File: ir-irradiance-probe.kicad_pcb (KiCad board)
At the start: 2 copper layers, 50 x 50 mm, 54 parts, among them J1 USB-C_UJC-HP-3-SMT-TR, J2 SM04B-SRSS-TB-LF-SN, J3 PinHeader_1x2_P2.54mm_Drill1.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, J4 Conn_BNC_031-70526-21, SW1 MSS3-V-T_R, U1 TLV70033_SC70, U2 AD8604ARUZ, U3 ADC101C027CIMK

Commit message: [#47284] Create local components library
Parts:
- C1, C10, C11, C2, C3, C4, C5, C7, C8, C9: footprint antmicro-footprints:C_0402_1005Metric -> ir-irradiance-probe-footprints:C_0402_1005Metric
- C6: footprint antmicro-footprints:C_0603_1608Metric -> ir-irradiance-probe-footprints:C_0603_1608Metric
- D1, D2, D3, D6: footprint antmicro-footprints:SOD-523 -> ir-irradiance-probe-footprints:SOD-523
- D4, D5: footprint antmicro-footprints:TPD2E009DRTR -> ir-irradiance-probe-footprints:TPD2E009DRTR
- D7: footprint antmicro-footprints:LED_0603_1608Metric_G -> ir-irradiance-probe-footprints:LED_0603_1608Metric_G
- D8, D9: footprint antmicro-footprints:Photodiode_SMD_4.2x5mm_TEMD -> ir-irradiance-probe-footprints:Photodiode_SMD_4.2x5mm_TEMD
- J1: footprint antmicro-footprints:USB-C_UJC-HP-3-SMT-TR -> ir-irradiance-probe-footprints:USB-C_UJC-HP-3-SMT-TR
- J2: footprint antmicro-footprints:SM04B-SRSS-TB-LF-SN -> ir-irradiance-probe-footprints:SM04B-SRSS-TB-LF-SN
- J3: footprint antmicro-footprints:PinHeader_1x2_P2.54_Drill0.9mm -> ir-irradiance-probe-footprints:PinHeader_1x2_P2.54_Drill0.9mm
- J4: footprint antmicro-footprints:Conn_BNC_031-70526-21 -> ir-irradiance-probe-footprints:Conn_BNC_031-70526-21
- L1: footprint antmicro-footprints:L_0603_1608Metric -> ir-irradiance-probe-footprints:L_0603_1608Metric
- MP1, MP2, MP3, MP4: footprint antmicro-footprints:mounting-hole-2.75mm-M2.5_D6.2mm_PTH -> ir-irradiance-probe-footprints:mounting-hole-2.75mm-M2.5_D6.2mm_PTH
- N1: footprint antmicro-footprints:antmicro-logo_scaled_20mm -> ir-irradiance-probe-footprints:antmicro-logo_scaled_20mm
- N2: footprint antmicro-footprints:oshw-logo -> ir-irradiance-probe-footprints:oshw-logo
- POT1: footprint antmicro-footprints:PTD902-1015K-B104 -> ir-irradiance-probe-footprints:PTD902-1015K-B104
- R1, R10, R11, R12, R13, R2, R3, R4, R5, R6, R7, R8, R9: footprint antmicro-footprints:R_0402_1005Metric -> ir-irradiance-probe-footprints:R_0402_1005Metric
- SW1: footprint antmicro-footprints:Switch_Slide_MSS3 -> ir-irradiance-probe-footprints:Switch_Slide_MSS3
- U1: footprint antmicro-footprints:SC-70-5 -> ir-irradiance-probe-footprints:SC-70-5
- U2: footprint antmicro-footprints:TSSOP-14_4.4x5mm_P0.65mm -> ir-irradiance-probe-footprints:TSSOP-14_4.4x5mm_P0.65mm
- U3: footprint antmicro-footprints:SOT-23-6 -> ir-irradiance-probe-footprints:SOT-23-6

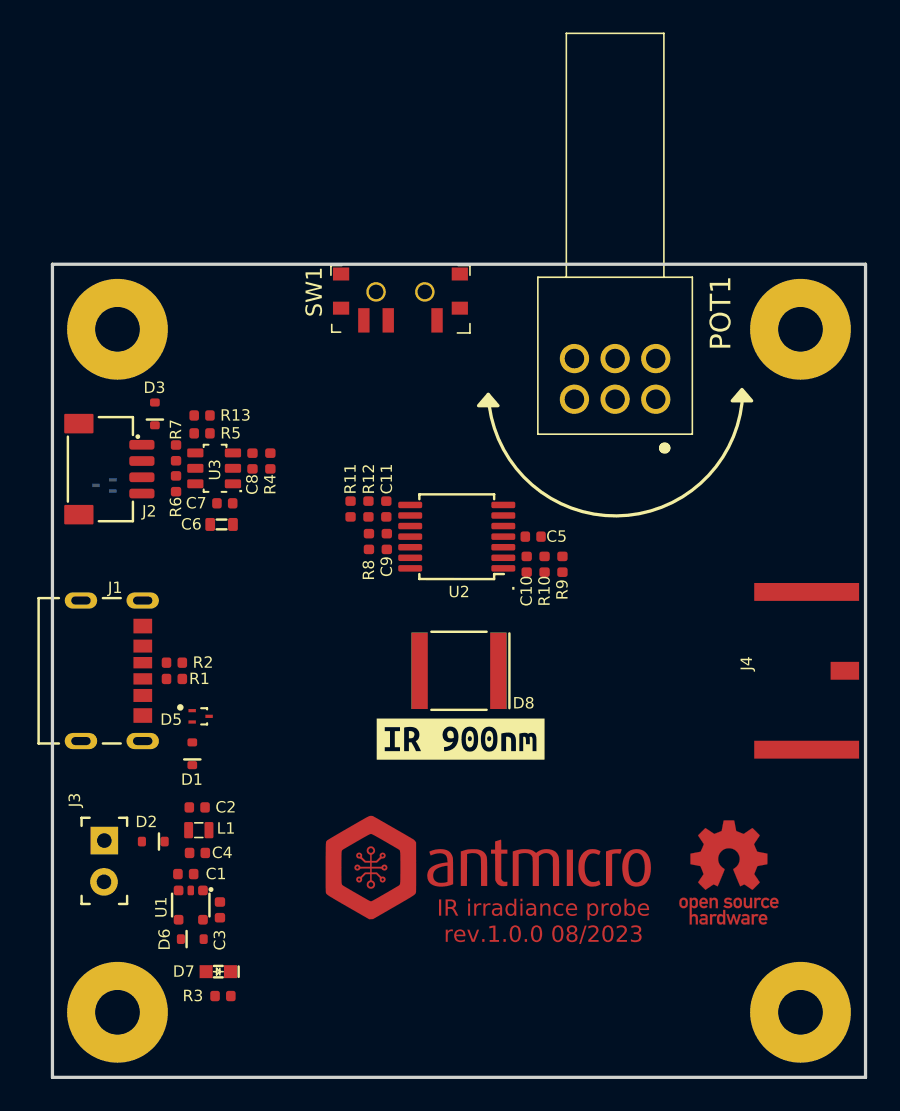
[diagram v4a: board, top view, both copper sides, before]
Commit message: [#47284] Rework PCB layout to fit 4x4cm board
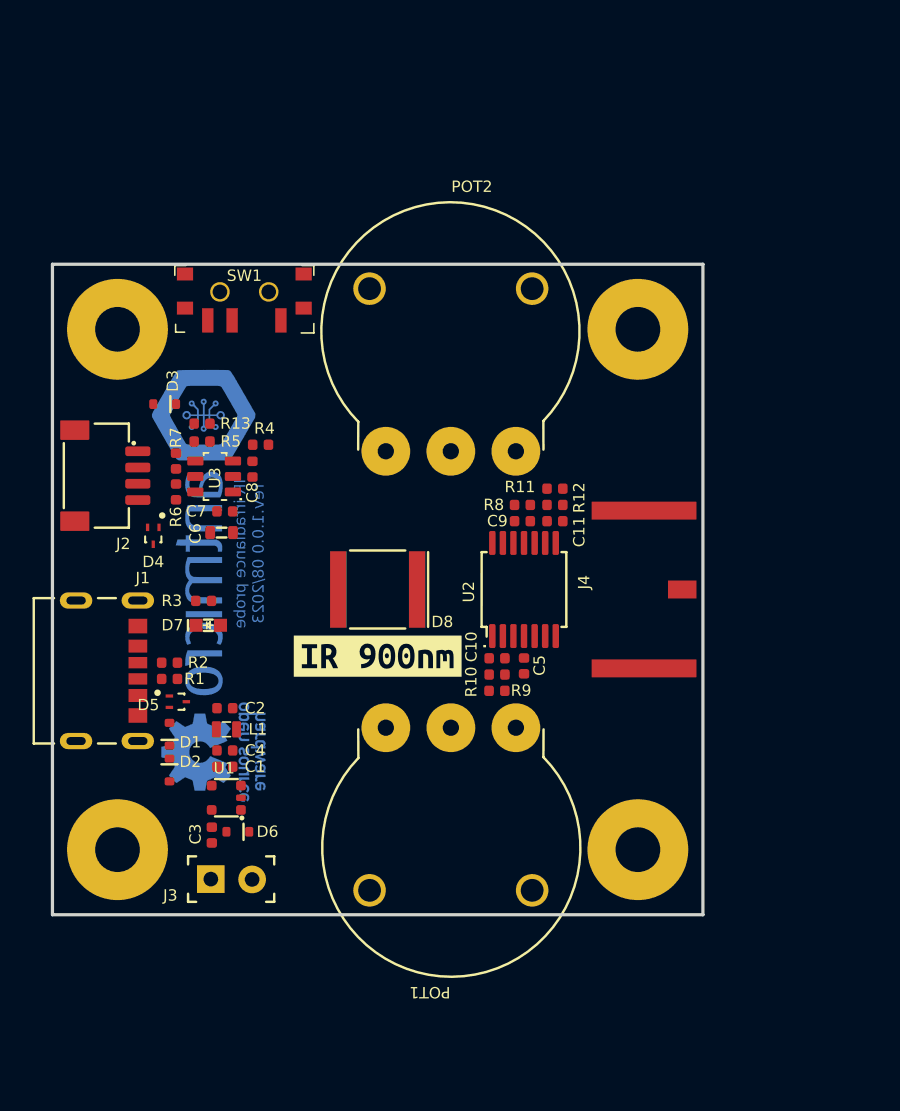
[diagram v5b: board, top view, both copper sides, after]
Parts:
- added POT2: POT_100k_R0141-2-100k, antmicro-footprints:POT_R0141-2, F.Cu at (90.5, 81.5)
- D4: moved to F.Cu
- N1, N2: moved to B.Cu
- POT1: value PTD902-1015K-B104 -> POT_100k_R0141-2-100k; footprint ir-irradiance-probe-footprints:PTD902-1015K-B104 -> antmicro-footprints:POT_R0141-2
- moved N2 32.6 mm to (79.9, 100.0), turned to -90 degrees
- moved N1 27.1 mm to (79.5, 86.5), turned to -90 degrees
- moved R3 24.3 mm to (79.3, 90.7), turned to 180 degrees
- moved POT1 22.0 mm to (98.5, 98.5), turned to 180 degrees
- moved D7 21.3 mm to (79.6, 92.2), turned to 180 degrees
- moved MP2 14.1 mm to (106.0, 106.0)
- moved R11 12.6 mm to (100.9, 83.8), turned to 0 degrees
- moved R12 11.5 mm to (100.9, 84.8), turned to 0 degrees
- moved J4 11.2 mm to (116.6, 90.0)
- moved C11 10.4 mm to (100.9, 85.8), turned to 0 degrees
- moved MP3 10.0 mm to (74.0, 106.0)
- moved MP4 10.0 mm to (106.0, 74.0)
- moved R8 9.70 mm to (98.9, 84.8), turned to 180 degrees
- moved SW1 9.60 mm to (81.8, 71.7)
- moved R9 8.76 mm to (97.3, 96.2), turned to 180 degrees
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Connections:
- R11 pad 2: Net-(POT1-Pad4) -> Net-(POT2-Pad1)
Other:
- board size 50 x 50 mm -> 40 x 40 mm

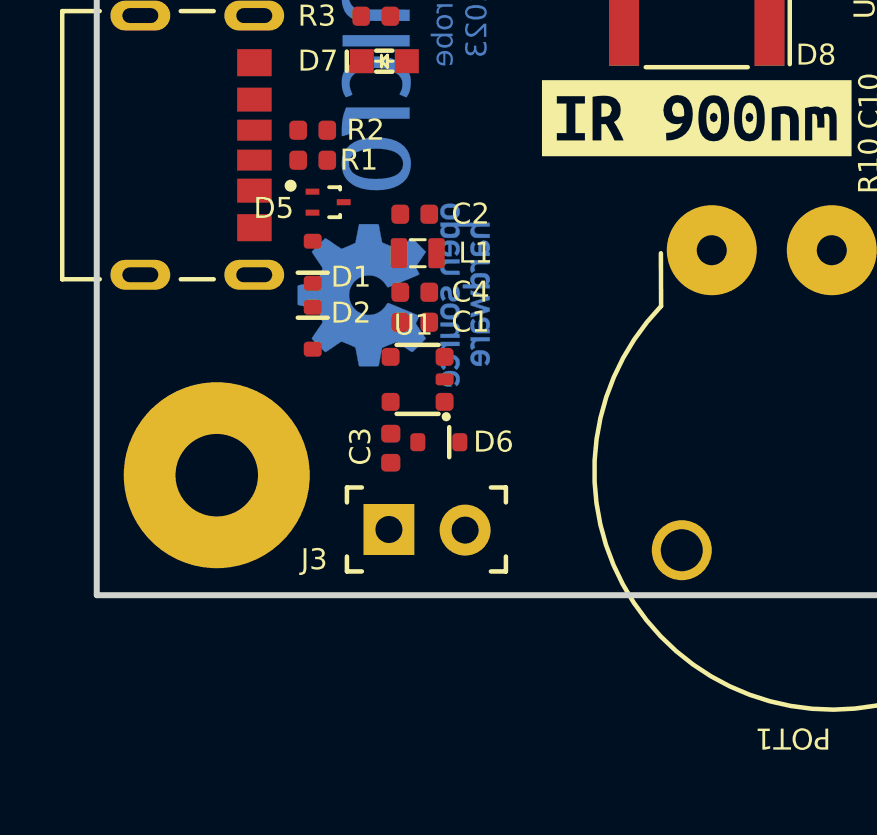
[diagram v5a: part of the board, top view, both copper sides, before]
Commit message: [#47284] Change pin header to horizontal
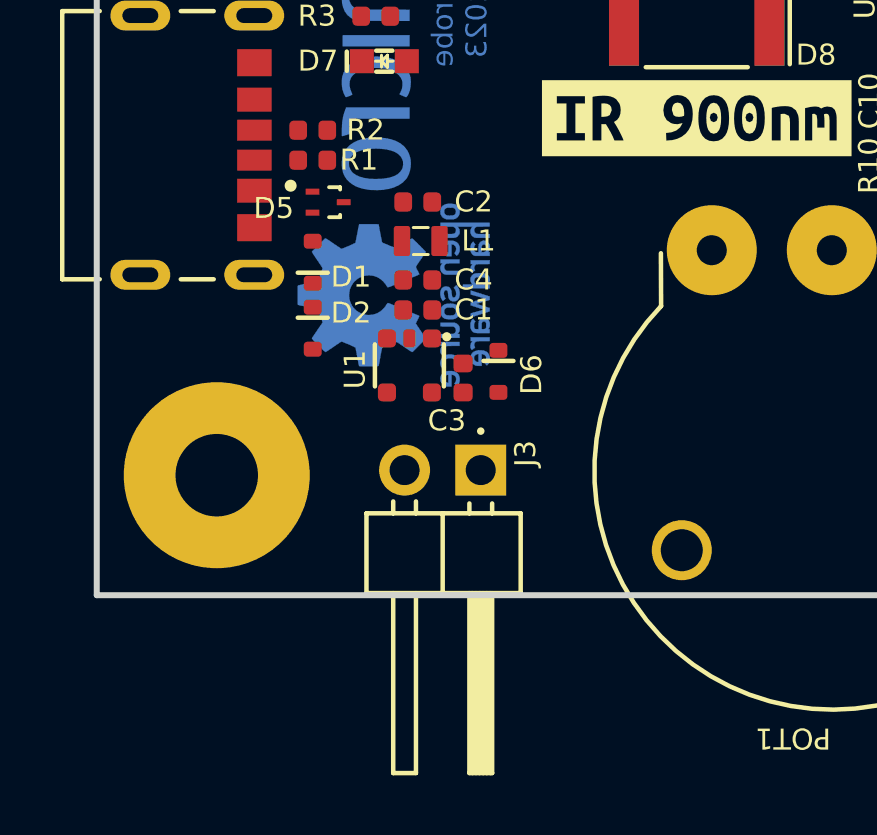
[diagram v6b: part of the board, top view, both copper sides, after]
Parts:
- J3: value PinHeader_1x2_P2.54mm_Drill1.1mm -> PinHeader_1x2_P2.54mm_Drill1.1mm_Horizontal; footprint ir-irradiance-probe-footprints:PinHeader_1x2_P2.54_Drill0.9mm -> ir-irradiance-probe-footprints:PinHeader_1x02_P2.54mm_Horizontal
- POT1, POT2: footprint antmicro-footprints:POT_R0141-2 -> ir-irradiance-probe-footprints:POT_R0141-2
- moved J3 3.64 mm to (82.8, 105.8), turned to -90 degrees
- moved C3 3.36 mm to (82.2, 102.8), turned to -90 degrees
- moved D6 3.09 mm to (83.4, 102.5), turned to -90 degrees
- moved U1 0.54 mm to (80.4, 102.3), turned to 180 degrees
- moved C1 0.42 mm to (80.7, 100.5)
- moved C4 0.42 mm to (80.7, 99.5)
- moved C2 0.42 mm to (80.7, 96.9)
- moved L1 0.42 mm to (80.8, 98.2)

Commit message: [#47284] Change bottom photodiode from TEMD5020X01 to TEMD5110X01
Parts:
- D9: value TEMD5020X01 -> TEMD5110X01; footprint ir-irradiance-probe-footprints:Photodiode_SMD_4.2x5mm_TEMD -> antmicro-footprints:Photodiode_SMD_4.2x5mm_TEMD

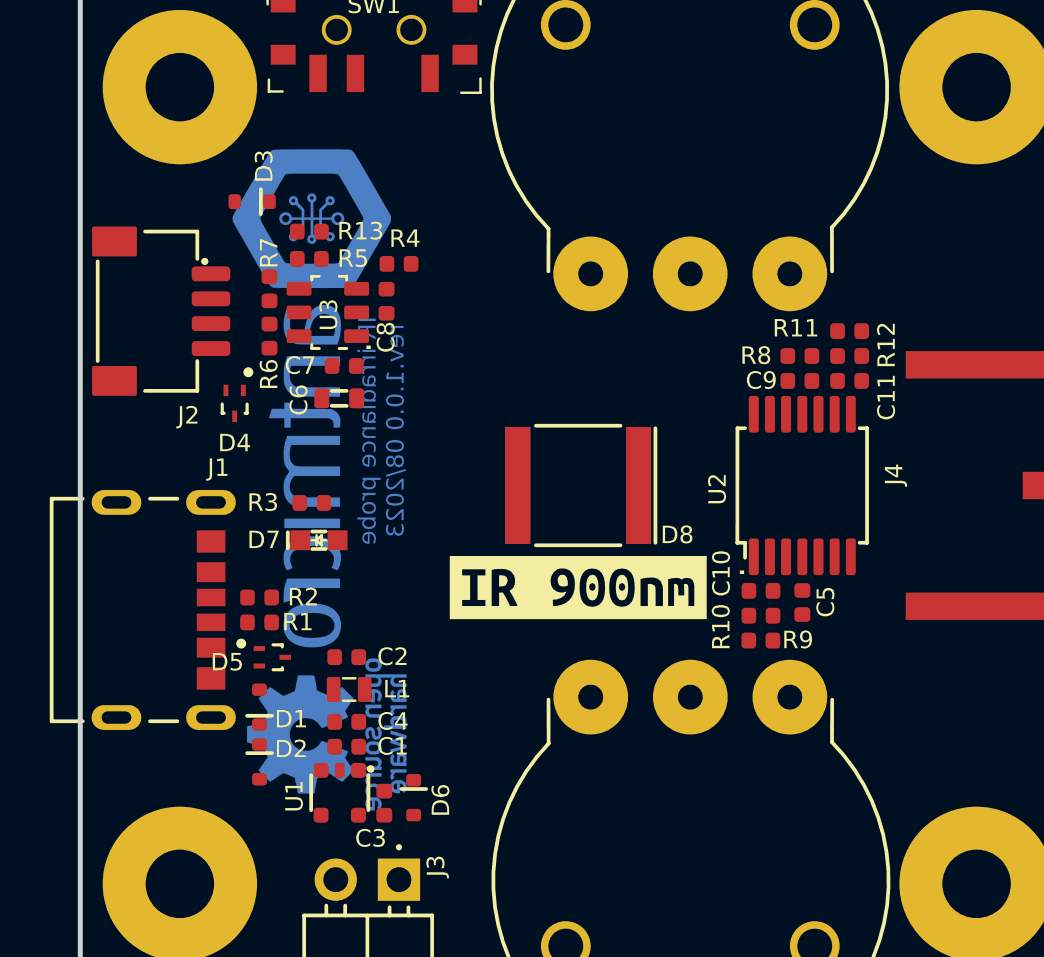
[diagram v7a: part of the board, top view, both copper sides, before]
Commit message: [#47284] Updated PCB layout
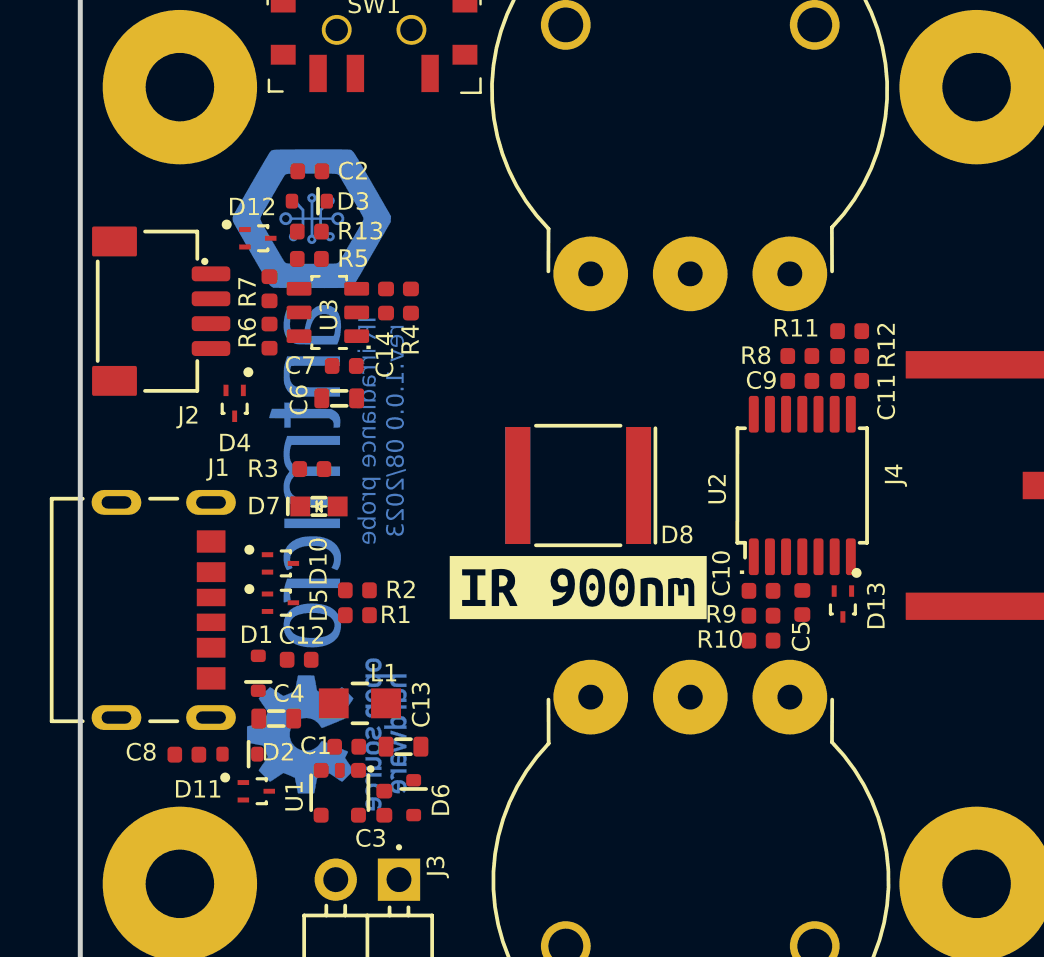
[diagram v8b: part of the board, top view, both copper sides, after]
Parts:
- added C12: C_100n_0402, antmicro-footprints:C_0402_1005Metric, F.Cu at (78.8, 97.0)
- added C13: C_10u_16V_0603, antmicro-footprints:C_0603_1608Metric, F.Cu at (83.0, 100.5)
- added C14: C_15n_0402, antmicro-footprints:C_0402_1005Metric, F.Cu at (82.3, 82.6)
- added D10: PESD5V0S2BQA, ir-irradiance-probe-footprints:TPD2E009DRTR, F.Cu at (78.0, 93.1)
- added D11: PESD5V0S2BQA, ir-irradiance-probe-footprints:TPD2E009DRTR, F.Cu at (77.1, 102.3)
- added D12: PESD5V0S2BQA, ir-irradiance-probe-footprints:TPD2E009DRTR, F.Cu at (77.1, 80.1)
- added D13: PESD5V0S2BQA, ir-irradiance-probe-footprints:TPD2E009DRTR, F.Cu at (100.6, 94.8)
- C2: value C_1u_0402 -> C_100n_0402; footprint ir-irradiance-probe-footprints:C_0402_1005Metric -> antmicro-footprints:C_0402_1005Metric
- C4: value C_1u_0402 -> C_10u_16V_0603; footprint ir-irradiance-probe-footprints:C_0402_1005Metric -> antmicro-footprints:C_0603_1608Metric
- C8: value C_470p_0402 -> C_100n_0402; footprint ir-irradiance-probe-footprints:C_0402_1005Metric -> antmicro-footprints:C_0402_1005Metric
- L1: value L_2u2_0.2A_0603 -> L_4u7_0.3A_0805; footprint ir-irradiance-probe-footprints:L_0603_1608Metric -> antmicro-footprints:L_0805_2012Metric
- R4: value R_22R_0402 -> R_1k_0402; footprint ir-irradiance-probe-footprints:R_0402_1005Metric -> antmicro-footprints:R_0402_1005Metric
- moved C8 19.9 mm to (74.3, 100.8), turned to 0 degrees
- moved C2 19.6 mm to (79.2, 77.4)
- moved R1 3.94 mm to (81.1, 95.2)
- moved R2 3.94 mm to (81.1, 94.2)
- moved C4 2.83 mm to (77.9, 99.4)
- moved D3 2.30 mm to (79.2, 78.6)
- moved D5 2.21 mm to (78.0, 94.7)
- moved R4 1.57 mm to (83.3, 82.6), turned to -90 degrees
- moved D1 1.36 mm to (77.2, 97.5)
- moved D7 1.36 mm to (79.6, 90.8)
- moved R3 1.36 mm to (79.3, 89.3)
- moved R9 1.00 mm to (97.3, 95.2)
- moved R10 1.00 mm to (97.3, 96.2)
- moved D2 0.85 mm to (76.4, 100.8), turned to 180 degrees
- moved L1 0.70 mm to (81.2, 98.8)
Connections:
- C2 pad 2: Net-(C2-Pad2) -> /3V3_JST
- C4 pad 2: /5V_FILTERED -> Net-(D1-Pad1)
- C8 pad 1: Net-(C8-Pad1) -> GND
- C8 pad 2: GND -> /5V_PWR_SUPPLY
- D1 pad 1: Net-(C2-Pad2) -> Net-(D1-Pad1)
- D2 pad 1: Net-(C2-Pad2) -> Net-(D1-Pad1)
- D5 pad 1: /5V_USB -> Net-(D5-Pad1)
- D5 pad 2: /5V_USB -> Net-(D5-Pad2)
- J1 pad A5: Net-(J1-PadA5) -> Net-(D5-Pad1)
- J1 pad B5: Net-(J1-PadB5) -> Net-(D5-Pad2)
- J3 pad 1: /5V_PWR_SUPPLY -> GND
- J3 pad 2: GND -> /5V_PWR_SUPPLY
- L1 pad 1: Net-(C2-Pad2) -> Net-(D1-Pad1)
- R1 pad 1: Net-(J1-PadB5) -> Net-(D5-Pad2)
- R2 pad 2: Net-(J1-PadA5) -> Net-(D5-Pad1)
- R4 pad 1: Net-(C8-Pad1) -> Net-(U3-Pad3)
- U3 pad 3: Net-(C8-Pad1) -> Net-(U3-Pad3)
